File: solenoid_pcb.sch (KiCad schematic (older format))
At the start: 17 parts, among them J1 VCC, J2 Programming, J3 Solenoid, Q1 IRF540NS, SW1 RESET, U1 LM2576S-3.3, U2 ESP-12F

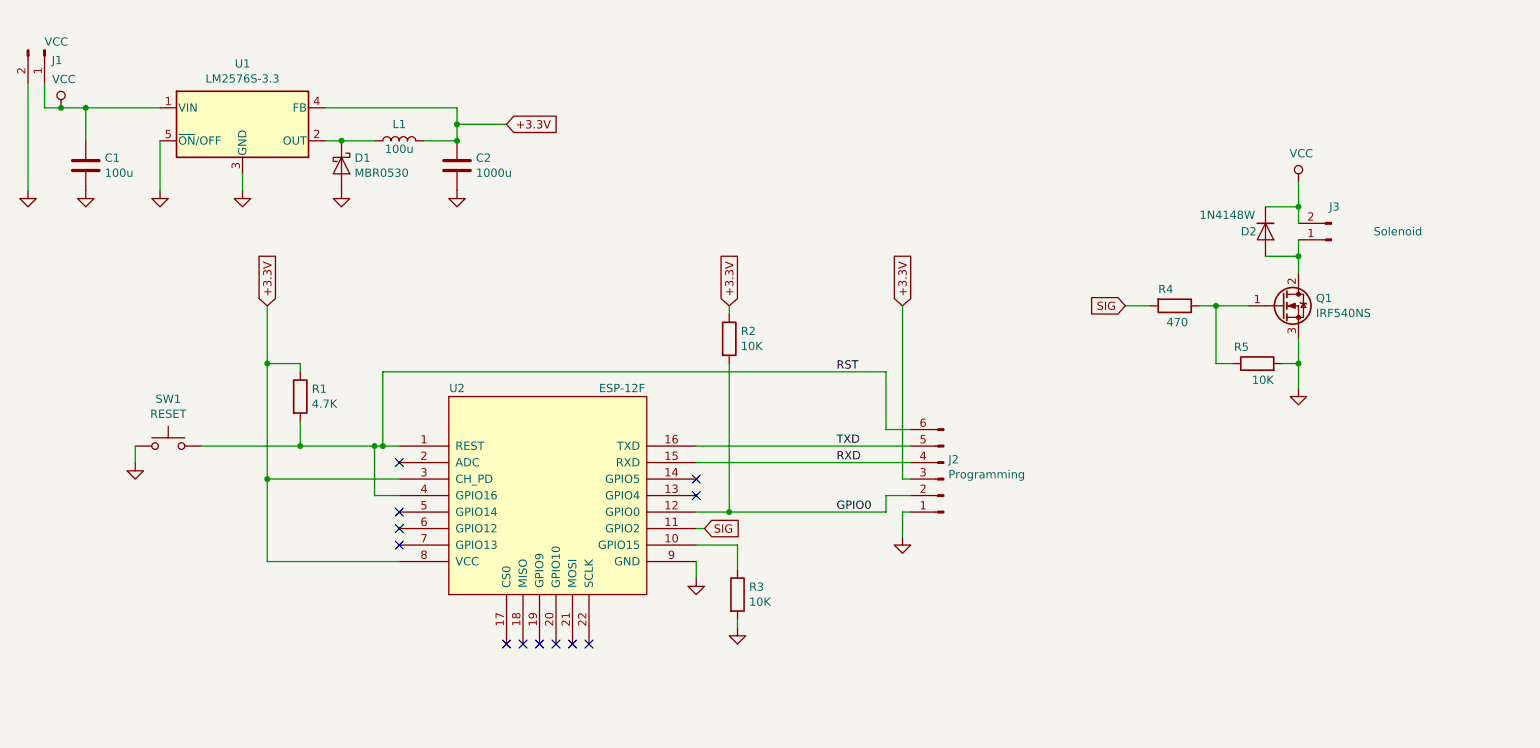
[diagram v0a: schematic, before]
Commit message: Dingen en zaken
3.3v heeft een eigen power symbol (ipv global label)
`sig` label locla gemaakt, kleinigheidje
2mm header is niet standaard! (2,54mm / 100mil wel)
Ook ff normale run-off-the-mill 6mm switch erin gestopt
Alle headers staan nu op het zelfde 2.54mm grid
Weet je zeker dat de footprint van je inductor klopt?
Zou je batterij input naast je dikke tor zetten, nu gaan je pulsen over je hele powerplane
Waarom eigen lijk over je hele board een powerplane op 12V, terwijl dat alleen door je fet gebruikt wordt?
Waar zijn die 6 gaten eigenlijk voor in't bordje? Schroeven zijn vaak groter zijn dan je denkt.. ;)
Heb ze er voor 't gemak ff uit gegooid, maar kunnen terug natuurlijk.
Verder nog wat via stiches erin stampen en wellicht nog wat decouple caps rond je ESP.
Enneuh.. ook handig (als 't een devbord is) om wat meer IO's richting header te voeren.. (ledje, input knoppies of miss zelfs een klein displaytje ofzo?)

ESP12 dingen:
Ben geswitched naar de stock (kicad) ESP12 symbol (git submodule lijkt te missen en is dus niet nodig)
Jouw ESP12 footprint is ook double sided, dat lijkt me nie zo handig.. Stock komponent lost ook dit op.
Weerstanden op GPIO0 en 15 volgens mij voor het booten/programmen van de ESP8266 dingetje?
GPIO02 moet je dacht ik naar vcc pullen, dus zou men solenoid ergens anders aan hangen.
GPIO16 aan reset, is dat een truuk om een software reset te doen? GPIO16 heeft een interne pull
down, dus weet niet offie dan lekker wil booten als je die aan RST hangt..
Anyway.. ken de ESP8266 niet zo goed, dus check vooral ff.. :) (Waarom eigenlijk niet 'n ESP32?)
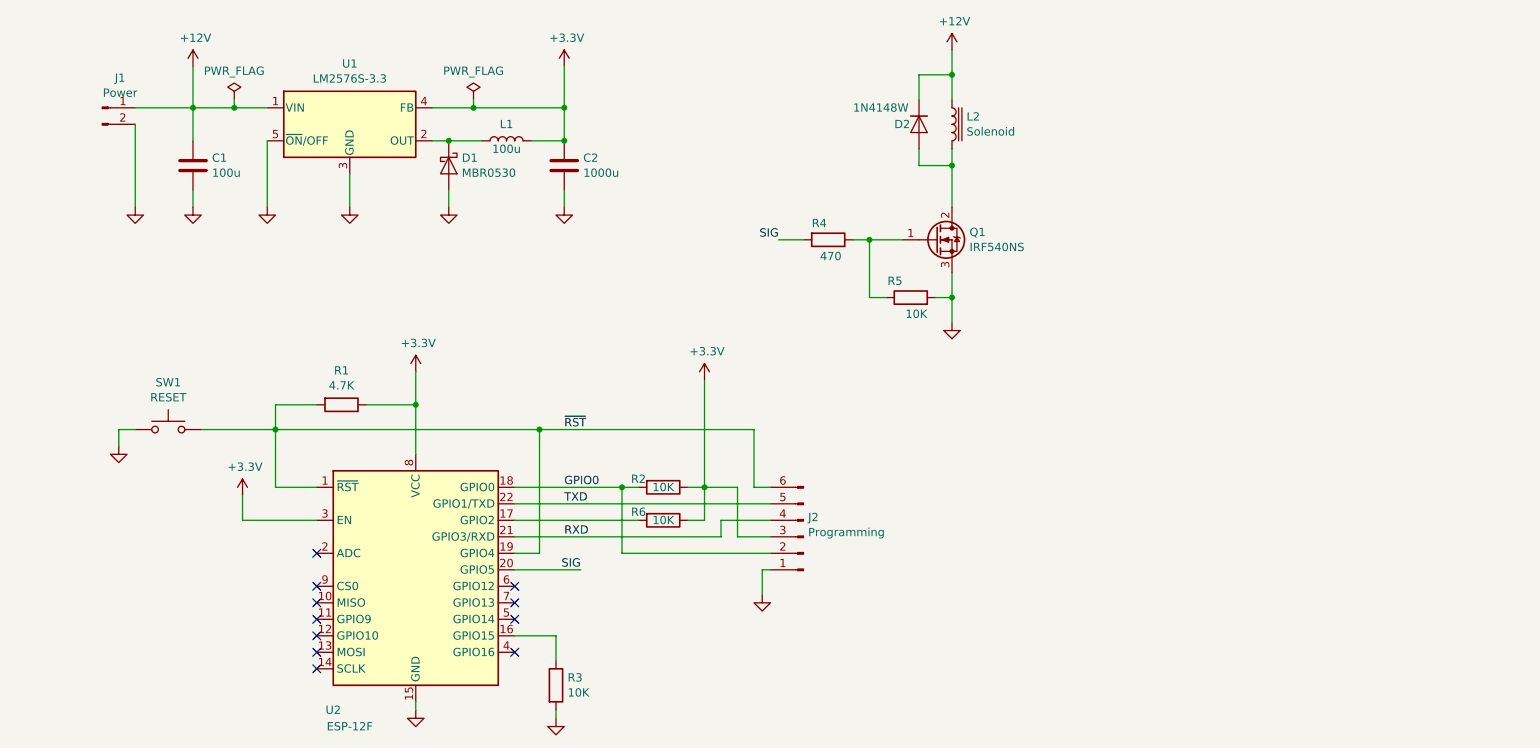
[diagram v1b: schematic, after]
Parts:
- removed J3: Solenoid, Connector_PinHeader_2.00mm:PinHeader_1x02_P2.00mm_Vertical, symbol Connector:Conn_01x02_Male
- removed U2: ESP-12F, ESP8266:ESP-12E, symbol ESP8266:ESP-12F
- added L2: Solenoid, Connector_PinHeader_2.54mm:PinHeader_1x02_P2.54mm_Vertical, symbol Device:L_Core_Iron
- added R6: 10K, Resistor_SMD:R_0805_2012Metric_Pad1.15x1.40mm_HandSolder, symbol Device:R
- added U2: ESP-12F, RF_Module:ESP-12E, symbol RF_Module:ESP-12F
- J1: value VCC -> Power; footprint Connector_PinHeader_2.00mm:PinHeader_1x02_P2.00mm_Vertical -> Connector_PinHeader_2.54mm:PinHeader_1x02_P2.54mm_Vertical
- J2: footprint Connector_PinHeader_2.00mm:PinHeader_1x06_P2.00mm_Vertical -> Connector_PinHeader_2.54mm:PinHeader_1x06_P2.54mm_Vertical
- SW1: footprint Button_Switch_SMD:SW_SPST_EVQPE1 -> Button_Switch_SMD:SW_SPST_PTS645
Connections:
- net GND: now also U2.15 (GND)
- net GPIO0: now also U2.18 (GPIO0)
- net RXD: now also U2.21 (GPIO3/RXD)
- net SIG: now also U2.20 (GPIO5)
- net TXD: now also U2.22 (GPIO1/TXD)
- net at R3.1: now also U2.16 (GPIO15)
- net at D2.2 (A), Q1.2 (D): now also L2.2
- net +3.3V renamed +3V3
- net +3V3: now also R6.1, U2.3 (EN), U2.8 (VCC)
- net RST renamed ~RST
- net ~RST: now also U2.1 (~RST), U2.19 (GPIO4)
- net VCC renamed +12V
- net +12V: now also L2.1
- new net: R6.2, U2.17 (GPIO2)
- no-connect marks 12 -> 11
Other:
- moved on the sheet: C1, C2, D1, D2, J1, J2, L1, Q1, R1, R2, R3, R4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

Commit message: Create smaller board, components to back (except ESP12), 2 channel output
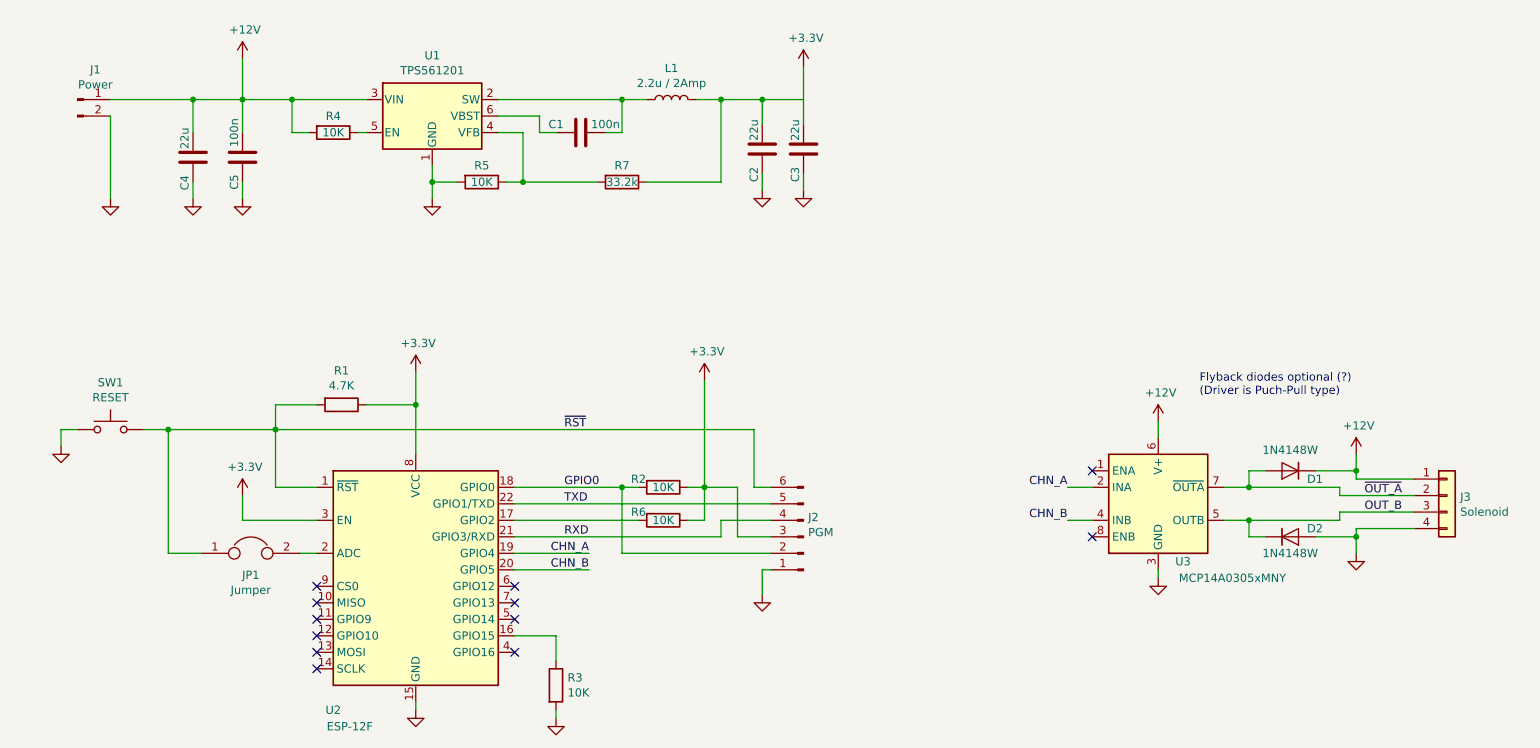
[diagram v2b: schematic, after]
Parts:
- removed D1: MBR0530, Diode_SMD:D_SOD-123, symbol Diode:MBR0530
- removed L2: Solenoid, Connector_PinHeader_2.54mm:PinHeader_1x02_P2.54mm_Vertical, symbol Device:L_Core_Iron
- removed Q1: IRF540NS, Package_TO_SOT_SMD:TO-263-2, symbol Transistor_FET:IRF540N
- removed U1: LM2576S-3.3, Package_TO_SOT_SMD:TO-263-5_TabPin3, symbol Regulator_Switching:LM2576S-3.3
- added C3, C4: 22u, Capacitor_SMD:C_0805_2012Metric, symbol Device:C
- added C5: 100n, Capacitor_SMD:C_0603_1608Metric, symbol Device:C
- added D1: 1N4148W, Diode_SMD:D_SOD-123, symbol Diode:1N4148W
- added J3: Solenoid, Connector_PinHeader_2.54mm:PinHeader_1x04_P2.54mm_Vertical, symbol Connector_Generic:Conn_01x04
- added JP1: Jumper, Jumper:SolderJumper-2_P1.3mm_Open_RoundedPad1.0x1.5mm, symbol Device:Jumper
- added R7: 33.2k, Resistor_SMD:R_0603_1608Metric, symbol Device:R
- added U1: TPS561201, Package_TO_SOT_SMD:SOT-23-6, symbol Regulator_Switching:TPS562200
- added U3: MCP14A0305xMNY, Package_DFN_QFN:WDFN-8-1EP_3x2mm_P0.5mm_EP1.3x1.4mm, symbol Driver_FET:MCP14A0305xMNY
- C1: value 100u -> 100n; footprint Capacitor_SMD:CP_Elec_6.3x5.4 -> Capacitor_SMD:C_0603_1608Metric
- C2: value 1000u -> 22u; footprint Capacitor_SMD:CP_Elec_10x10.5 -> Capacitor_SMD:C_0805_2012Metric
- J2: value Programming -> PGM
- L1: value 100u -> 2.2u / 2Amp; footprint Inductor_SMD:L_7.3x7.3_H4.5 -> Inductor_SMD:L_Bourns-SRN4018
- R1, R2, R3, R5, R6: footprint Resistor_SMD:R_0805_2012Metric_Pad1.15x1.40mm_HandSolder -> Resistor_SMD:R_0603_1608Metric
- R4: value 470 -> 10K; footprint Resistor_SMD:R_0805_2012Metric_Pad1.15x1.40mm_HandSolder -> Resistor_SMD:R_0603_1608Metric
- SW1: footprint Button_Switch_SMD:SW_SPST_PTS645 -> Button_Switch_SMD:SW_SPST_B3U-1000P-B
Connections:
- net +12V: now also R4.2, C4.1, C5.1, D1.1 (K), J3.1 (Pin_1), U1.3 (VIN), U3.6 (V+); no longer C1.1, D2.1 (K)
- net +3V3: now also C3.1, R7.1
- net GND: now also D2.2 (A), C3.2, C4.2, C5.2, J3.4 (Pin_4), U1.1 (GND), U3.3 (GND), U3.9 (GND); no longer C1.2
- net ~RST: now also JP1.1; no longer U2.19 (GPIO4)
- net at L1.1: now also C1.1, U1.2 (SW)
- net at R5.1: now also R7.2, U1.4 (VFB); no longer R4.1
- net at U2.2 (ADC): now also JP1.2
- net SIG renamed CHN_B
- net CHN_B: now also U3.4 (INB); no longer R4.2
- new net: R4.1, U1.5 (EN)
- new net: C1.2, U1.6 (VBST)
- new net CHN_A: U2.19 (GPIO4), U3.2 (INA)
- new net OUT_B: D2.1 (K), J3.3 (Pin_3), U3.5 (OUTB)
- new net ~OUT_A: D1.2 (A), J3.2 (Pin_2), U3.7 (~OUTA)
- no-connect marks 11 -> 12
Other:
- note added: "Flyback diodes optional (?)\n(Driver is Puch-Pull type)"
- moved on the sheet: J1, L1, SW1
